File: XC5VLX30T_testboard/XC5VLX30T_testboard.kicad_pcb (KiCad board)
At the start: 4 copper layers, 99 x 99 mm, 28 parts, among them J1 Conn_01x35_Pin, J10 Conn_01x04_Pin, J11 Conn_01x04_Pin, J12 Conn_01x04_Pin, J13 Conn_01x04_Pin, J14 Conn_01x04_Pin, J2 Conn_01x35_Pin, J3 Conn_01x35_Pin, J4 Conn_01x35_Pin, J5 Conn_01x35_Pin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

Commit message: more clicking
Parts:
- moved C6 10.2 mm to (158.2, 122.4), turned to 180 degrees
- moved C5 8.01 mm to (152.1, 122.4), turned to 0 degrees
- moved C9 7.96 mm to (177.4, 122.5), turned to 0 degrees
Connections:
- J10 pad 1: VccAUX -> GND
- J10 pad 2: VccAUX -> GND
- J11 pad 1: unconnected-(J11-Pin_1-Pad1) -> vccext
- J11 pad 2: unconnected-(J11-Pin_2-Pad2) -> vccext
- J11 pad 3: unconnected-(J11-Pin_3-Pad3) -> GND
- J11 pad 4: unconnected-(J11-Pin_4-Pad4) -> GND
- J12 pad 1: VCCO -> GND
- J12 pad 2: VCCO -> GND
- J13 pad 1: unconnected-(J13-Pin_1-Pad1) -> vccext
- J13 pad 2: unconnected-(J13-Pin_2-Pad2) -> vccext
- J13 pad 3: unconnected-(J13-Pin_3-Pad3) -> GND
- J13 pad 4: unconnected-(J13-Pin_4-Pad4) -> GND
- J14 pad 1: VccINT -> GND
- J14 pad 2: VccINT -> GND
- J9 pad 1: unconnected-(J9-Pin_1-Pad1) -> vccext
- J9 pad 2: unconnected-(J9-Pin_2-Pad2) -> vccext
- J9 pad 3: unconnected-(J9-Pin_3-Pad3) -> GND
- J9 pad 4: unconnected-(J9-Pin_4-Pad4) -> GND
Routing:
- net vccext: track 0.00 -> 88.0 mm
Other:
- board text added: "VCCAUX"
- board text added: "VCCO"

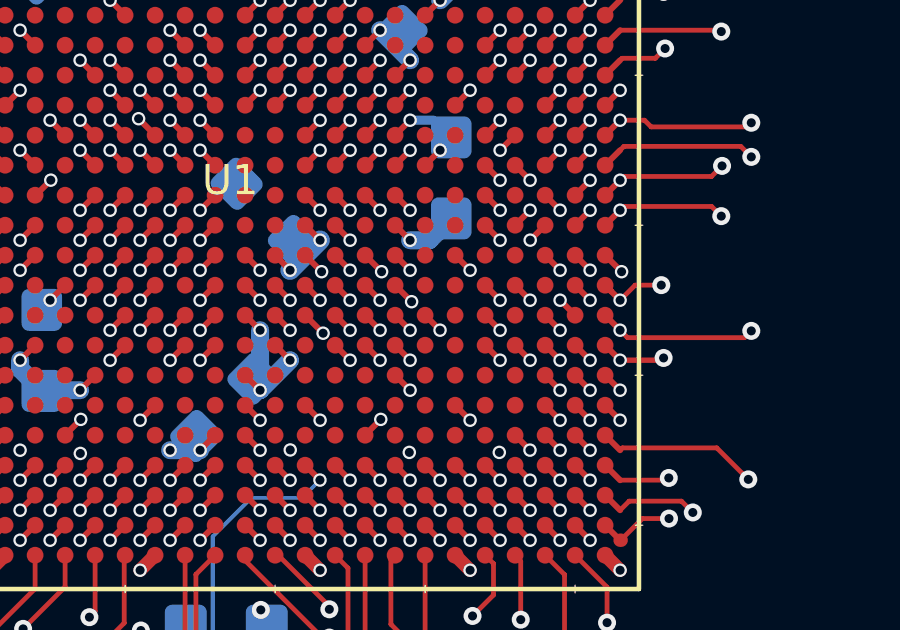
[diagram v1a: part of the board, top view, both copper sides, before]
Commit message: mode select pins + pull down resistors
"If the Virtex-5 device is configured via JTAG on power-up, it is advisable to tie the mode pins to the Boundary-Scan configuration mode settings: 101 (M2 = 1, M1 = 0,
M0 = 1)."
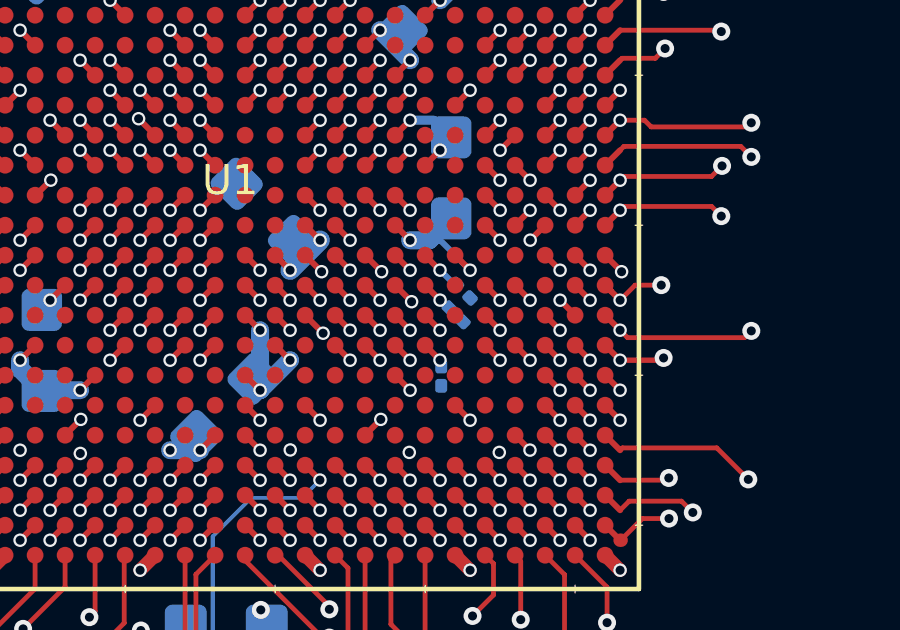
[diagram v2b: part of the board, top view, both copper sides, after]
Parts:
- added R1: R, Resistor_SMD:R_0201_0603Metric, B.Cu at (171.4, 153.6)
- added R2: R, Resistor_SMD:R_0201_0603Metric, B.Cu at (171.9, 151.6)
- added R3: R, Resistor_SMD:R_0201_0603Metric, B.Cu at (172.2, 150.8)
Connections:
- U1 pad T20: unconnected-(U1F-M0_0-PadT20) -> M0_MODESELECT
- U1 pad U20: unconnected-(U1F-M2_0-PadU20) -> M2_MODESELECT
- U1 pad W20: unconnected-(U1F-M1_0-PadW20) -> M1_MODESELECT
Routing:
- net GND: track 124.5 -> 126.2 mm
- net M0_MODESELECT: track 0.00 -> 1.44 mm, vias 0 -> 1
- net M2_MODESELECT: track 0.00 -> 1.12 mm, vias 0 -> 1
- net M1_MODESELECT: track 0.00 -> 0.70 mm, vias 0 -> 1

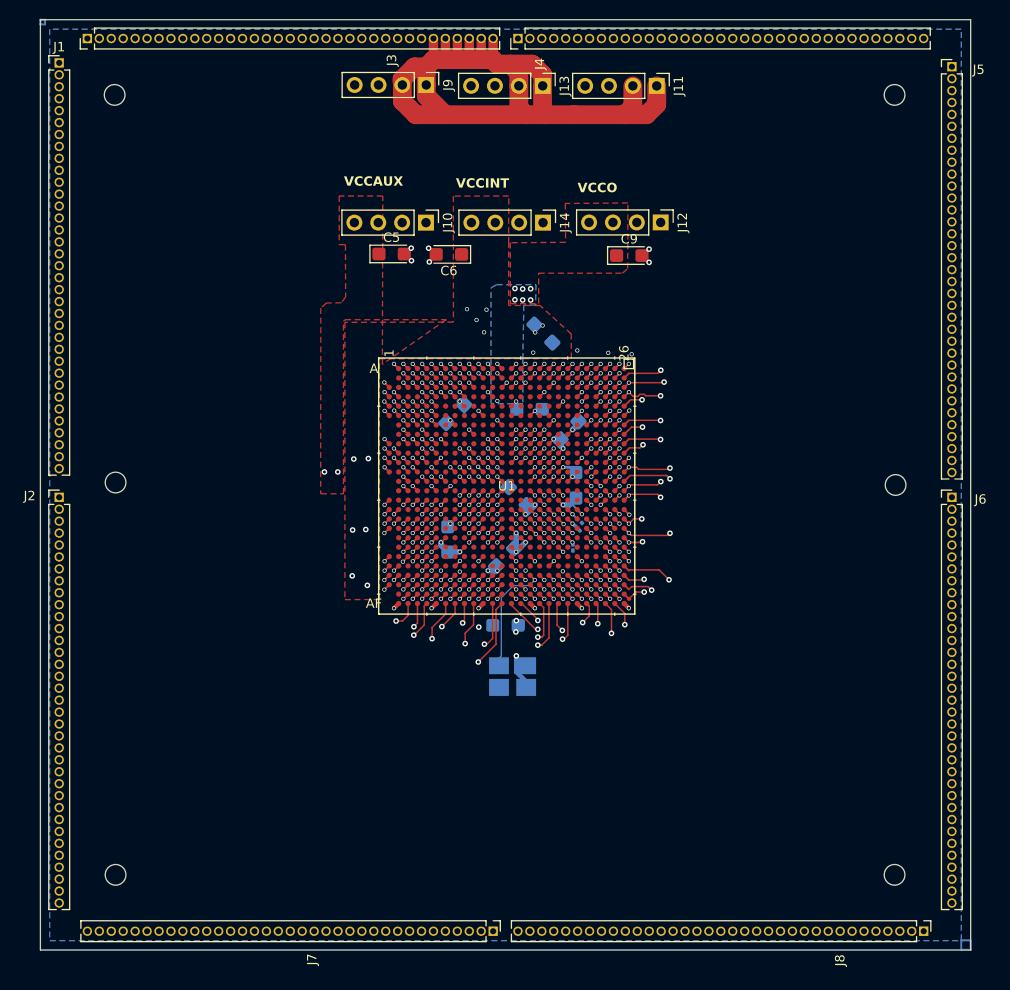
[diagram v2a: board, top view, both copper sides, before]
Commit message: resize wires to .13mm
resized wires to 0.13mm
added top layer gnd plane, vccaux plane
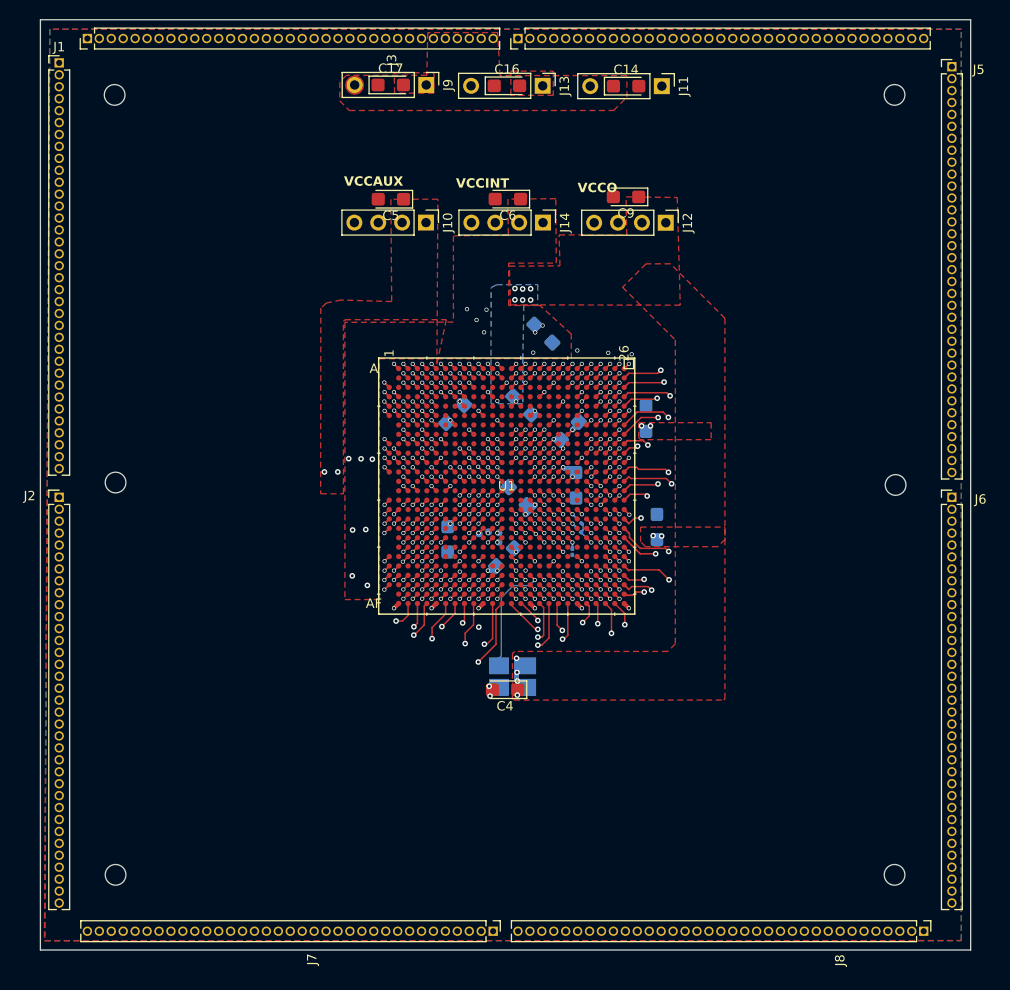
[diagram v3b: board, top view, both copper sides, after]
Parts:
- added C10: 470uF, Capacitor_Tantalum_SMD:CP_EIA-3216-12_Kemet-S, B.Cu at (180.4, 151.4)
- added C11: 470uF, Capacitor_Tantalum_SMD:CP_EIA-3216-12_Kemet-S, B.Cu at (179.2, 139.9)
- added C14: 470uF, Capacitor_Tantalum_SMD:CP_EIA-3216-12_Kemet-S, F.Cu at (177.1, 104.5)
- added C16: 470uF, Capacitor_Tantalum_SMD:CP_EIA-3216-12_Kemet-S, F.Cu at (164.4, 104.5)
- added C17: 470uF, Capacitor_Tantalum_SMD:CP_EIA-3216-12_Kemet-S, F.Cu at (152.1, 104.4)
- added TP1: TestPoint, Connector_Pin:Pin_D0.7mm_L6.5mm_W1.8mm_FlatFork, B.Cu at (162.5, 151.9)
- added TP2: TestPoint, Connector_Pin:Pin_D0.7mm_L6.5mm_W1.8mm_FlatFork, B.Cu at (161.5, 152.1)
- added TP3: TestPoint, Connector_Pin:Pin_D0.7mm_L6.5mm_W1.8mm_FlatFork, B.Cu at (163.6, 152.0)
- added TP4: TestPoint, Connector_Pin:Pin_D0.7mm_L6.5mm_W1.8mm_FlatFork, B.Cu at (163.6, 153.0)
- C4: moved to F.Cu
- moved C6 8.61 mm to (164.5, 116.5)
- moved C4 6.85 mm to (164.2, 168.7)
- moved C9 6.25 mm to (177.1, 116.3), turned to 180 degrees
- moved C5 5.83 mm to (152.1, 116.5), turned to 180 degrees
- moved C13 0.88 mm to (166.0, 138.5), turned to -45 degrees
- moved J11 0.54 mm to (180.9, 104.5)
- moved J12 0.54 mm to (181.3, 119.0)
- moved R1 0.47 mm to (171.4, 154.1)
- moved R2 0.25 mm to (172.1, 151.8)
- moved C2 0.07 mm to (171.1, 141.2)
- moved R3 0.06 mm to (172.1, 150.8)
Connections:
- J10 pad 1: GND -> VccAUX
- J10 pad 2: GND -> VccAUX
- J10 pad 3: VccAUX -> GND
- J10 pad 4: VccAUX -> GND
- J11 pad 1: vccext -> GND
- J11 pad 4: GND -> vccext
- J12 pad 1: GND -> VCCO
- J12 pad 2: GND -> VCCO
- J12 pad 3: VCCO -> GND
- J12 pad 4: VCCO -> GND
- J13 pad 1: vccext -> GND
- J13 pad 4: GND -> vccext
- J14 pad 1: GND -> VccINT
- J14 pad 2: GND -> VccINT
- J14 pad 3: VccINT -> GND
- J14 pad 4: VccINT -> GND
- J6 pad 30: IO_L9P_CC_SM0P_13 -> IO_L8N_CC_SM1N_13
- J6 pad 31: IO_L8P_CC_SM1P_13 -> IO_L9P_CC_SM0P_13
- J6 pad 32: IO_L8N_CC_SM1N_13 -> IO_L8P_CC_SM1P_13
- J9 pad 1: vccext -> GND
- J9 pad 4: GND -> vccext
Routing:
- net vccext: track 88.0 -> 0.04 mm
- net GND: track 126.2 -> 115.8 mm, vias 167 -> 163
- net VCCO: track 75.5 -> 66.1 mm, vias 47 -> 52
- net IO_L0P_SM8P_13: track 46.0 -> 41.5 mm, vias 2 -> 1
- net IO_L19P_SM9P_11: track 49.2 -> 45.6 mm
- net IO_L8N_CC_SM1N_13: track 53.2 -> 49.7 mm
- net IO_L1P_SM7P_13: track 45.9 -> 43.2 mm
- net IO_L7N_GC_VRP: track 49.1 -> 51.4 mm
- net IO_L2N_15: track 58.4 -> 56.6 mm
- net IO_L16N_17: track 46.5 -> 48.2 mm
- net IO_L1P_15: track 60.0 -> 58.3 mm
- net IO_L3P_15: track 58.4 -> 56.7 mm
- net IO_L2P_15: track 59.5 -> 57.9 mm
- net IO_L2P_SM6P_13: track 46.4 -> 44.9 mm
- net VccINT: track 35.4 -> 33.9 mm, vias 59 -> 60
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- added copper zone on F.Cu, net GND
- added copper zone on F.Cu, net vccext

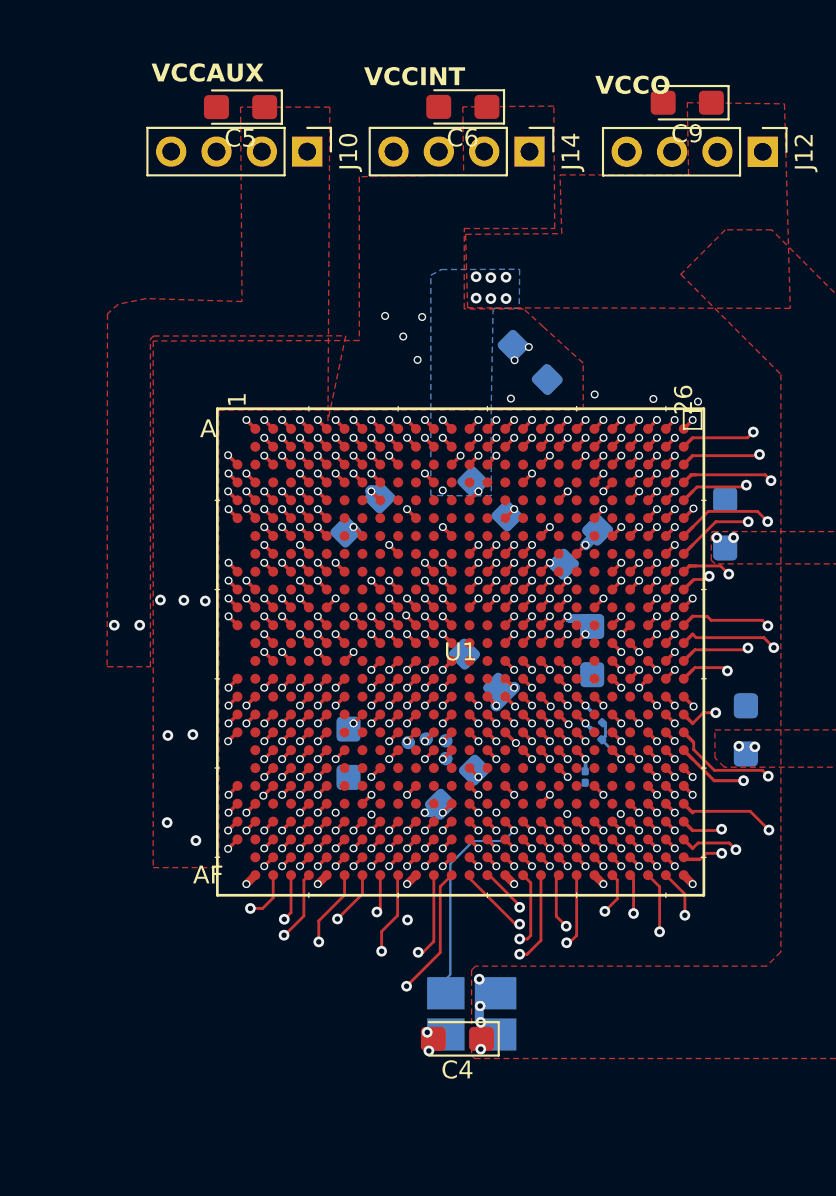
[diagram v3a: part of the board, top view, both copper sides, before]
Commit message: moved clock to P from N
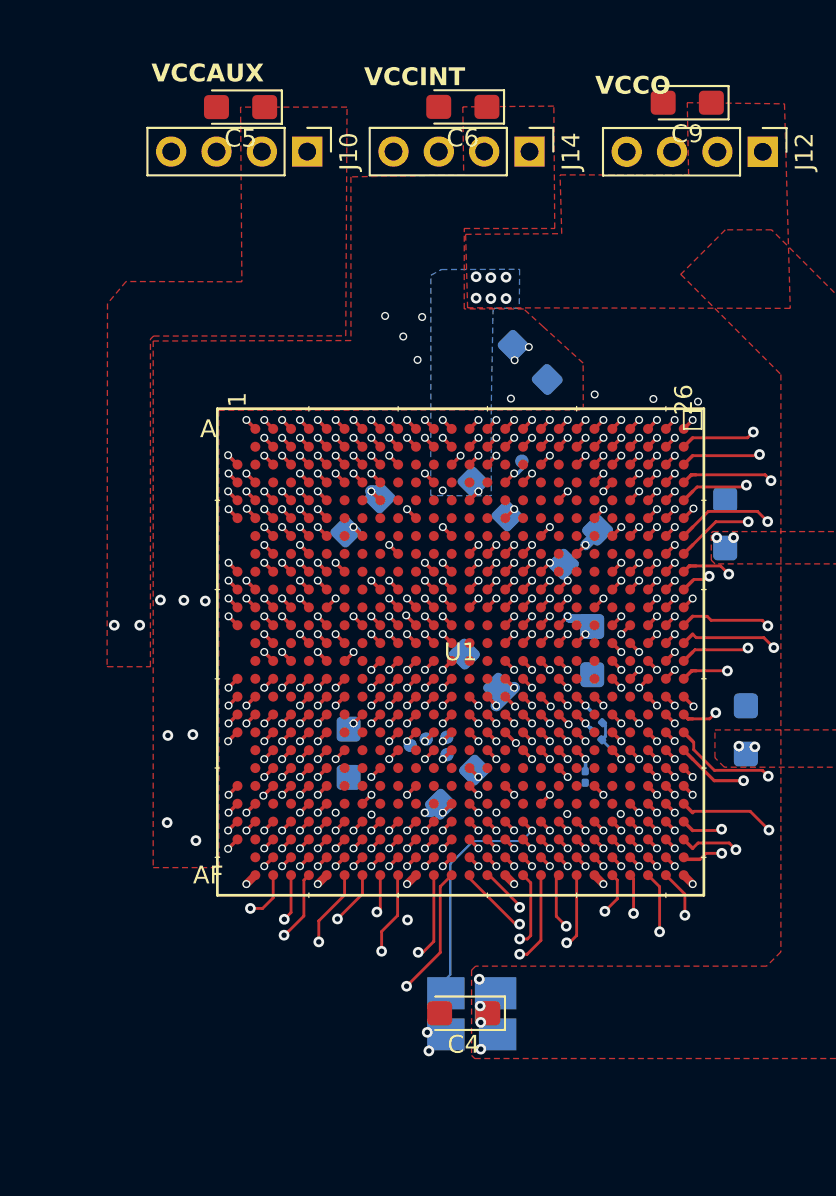
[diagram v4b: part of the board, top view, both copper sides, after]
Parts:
- added TP5: TestPoint, Connector_Pin:Pin_D0.7mm_L6.5mm_W1.8mm_FlatFork, B.Cu at (167.8, 136.4)
- moved C4 1.48 mm to (164.6, 167.3)
- moved TP4 0.23 mm to (163.6, 152.8)
- moved TP3 0.21 mm to (163.6, 151.8)
- moved TP2 0.19 mm to (161.6, 152.3)
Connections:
- U1 pad AC16: CLK -> IO_L8P_CC_GC_4
- U1 pad AC17: IO_L8P_CC_GC_4 -> CLK
- U1 pad D16: unconnected-(U1C-IO_L1P_CC_GC_3-PadD16) -> CLK_AUX1
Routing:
- net CLK_AUX1: track 0.00 -> 1.68 mm, vias 0 -> 1
- net CLK: track 11.8 -> 12.8 mm
- net IO_L8P_CC_GC_4: track 44.9 -> 45.7 mm
